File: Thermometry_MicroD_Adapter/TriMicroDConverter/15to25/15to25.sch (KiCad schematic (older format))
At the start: 3 parts, among them J1 Conn_02x05_Odd_Even, J2 DB15_Male, J4 DB25_Male

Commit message: update
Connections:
- net at J2.3: no longer J4.3
- net at J2.4: now also J4.3; no longer J4.4
- net at J2.5: now also J4.4; no longer J4.5
- net at J2.6: now also J4.5; no longer J4.6
- net at J2.7: now also J4.6
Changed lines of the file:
@@
 $EndComp
 Wire Wire Line
-	6500 2000 5950 2000
-Wire Wire Line
-	6500 2100 5950 2100
-Wire Wire Line
-	5950 2200 6500 2200
-Wire Wire Line
-	6500 2300 5950 2300
-Wire Wire Line
-	5950 2400 6500 2400
-Wire Wire Line
-	6500 2500 5950 2500
-Wire Wire Line
-	5950 2600 6500 2600
-Wire Wire Line
-	6500 2700 5950 2700
-Wire Wire Line
-	5950 2800 6500 2800
-Wire Wire Line
-	6500 2900 5950 2900
-Wire Wire Line
-	5950 3000 6500 3000
-Wire Wire Line
-	6500 3100 5950 3100
-Wire Wire Line
-	6500 3300 6700 3300
-Wire Wire Line
-	6700 3300 6700 3150
-Wire Wire Line
-	6700 3150 6100 3150
-Wire Wire Line
-	6100 3150 6100 3300
-Wire Wire Line
-	6100 3300 5950 3300
-NoConn ~ 5950 3200
-Wire Wire Line
-	6150 3200 6150 3350
-Wire Wire Line
-	6150 3350 5950 3350
-Wire Wire Line
 	5950 3350 5950 3400
-Wire Wire Line
-	6150 3200 6500 3200
 NoConn ~ 6500 4400
 $Comp
@@
 Wire Wire Line
 	5300 3800 5300 3750
+NoConn ~ 5950 2400
+Wire Wire Line
+	5950 2000 6500 2000
+Wire Wire Line
+	5950 2100 6500 2100
+Wire Wire Line
+	5950 2200 6500 2200
+Wire Wire Line
+	5950 2300 6500 2300
+Wire Wire Line
+	6500 2400 6150 2400
+Wire Wire Line
+	6150 2400 6150 2600
+Wire Wire Line
+	6150 2600 5950 2600
+Wire Wire Line
+	5950 2500 6500 2500
+Wire Wire Line
+	6500 2600 6200 2600
+Wire Wire Line
+	6200 2600 6200 2800
+Wire Wire Line
+	6200 2800 5950 2800
+Wire Wire Line
+	5950 2700 6500 2700
+Wire Wire Line
+	6500 2800 6250 2800
+Wire Wire Line
+	6250 2800 6250 3000
+Wire Wire Line
+	6250 3000 5950 3000
+Wire Wire Line
+	5950 2900 6500 2900
+Wire Wire Line
+	6500 3000 6300 3000
+Wire Wire Line
+	6300 3000 6300 3200
+Wire Wire Line
+	6300 3200 5950 3200
+Wire Wire Line
+	5950 3100 6500 3100
+Wire Wire Line
+	6500 3200 6350 3200
+Wire Wire Line
+	6350 3200 6350 3350
+Wire Wire Line
+	6350 3350 5950 3350
+Wire Wire Line
+	5950 3300 6500 3300
 $EndSCHEMATC

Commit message: update
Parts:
- removed J1: Conn_02x05_Odd_Even, Connector_PinHeader_1.00mm:PinHeader_2x05_P1.00mm_Vertical, symbol Connector_Generic:Conn_02x05_Odd_Even
- added J1, J3: Conn_01x04, Connector_JST:JST_PH_B4B-PH-K_1x04_P2.00mm_Vertical, symbol Connector_Generic:Conn_01x04
- added J5: Conn_01x02, Connector_PinHeader_1.00mm:PinHeader_1x02_P1.00mm_Vertical, symbol Connector_Generic:Conn_01x02
- J2: symbol Connector:DB15_Male -> Connector:DB15_Male_MountingHoles
- J4: symbol Connector:DB25_Male -> Connector:DB25_Male_MountingHoles
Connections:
- net at J4.10: now also J3.1 (Pin_1)
- net at J4.11: now also J3.3 (Pin_3)
- net at J4.12: now also J5.1 (Pin_1)
- net at J4.21 (P21): now also J1.2 (Pin_2)
- net at J4.22 (P22): now also J1.4 (Pin_4)
- net at J4.23 (P23): now also J3.2 (Pin_2)
- net at J4.24 (P24): now also J3.4 (Pin_4)
- net at J4.25 (P25): now also J5.2 (Pin_2)
- net at J4.8: now also J1.1 (Pin_1)
- net at J4.9: now also J1.3 (Pin_3)
- new net GND: J2.0 (PAD), J4.0 (PAD)
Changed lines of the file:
@@
 $EndDescr
 $Comp
-L Connector:DB25_Male J4
+L Connector:DB25_Male_MountingHoles J4
 U 1 1 610858EB
 P 6800 3200
@@
 $EndComp
 Wire Wire Line
+	6500 2000 5950 2000
+Wire Wire Line
+	6500 2100 5950 2100
+Wire Wire Line
+	5950 2200 6500 2200
+Wire Wire Line
+	6500 2300 5950 2300
+Wire Wire Line
+	6500 2500 5950 2500
+Wire Wire Line
+	6500 2700 5950 2700
+Wire Wire Line
+	6500 2900 5950 2900
+Wire Wire Line
+	6500 3100 5950 3100
+Wire Wire Line
 	5950 3350 5950 3400
 NoConn ~ 6500 4400
 $Comp
-L Connector_Generic:Conn_02x05_Odd_Even J1
-U 1 1 610B8918
-P 5600 3950
-F 0 "J1" H 5650 4367 50  0000 C CNN
-F 1 "Conn_02x05_Odd_Even" H 5650 4276 50  0000 C CNN
-F 2 "Connector_PinHeader_1.00mm:PinHeader_2x05_P1.00mm_Vertical" H 5600 3950 50  0001 C CNN
-F 3 "~" H 5600 3950 50  0001 C CNN
-	1    5600 3950
-	-1   0    0    -1
-$EndComp
-$Comp
-L Connector:DB15_Male J2
+L Connector:DB15_Male_MountingHoles J2
 U 1 1 61081BFB
 P 5650 2700
@@
 	6000 3400 6000 3750
 Wire Wire Line
-	6000 3750 5800 3750
-Wire Wire Line
 	6500 3600 6100 3600
-Wire Wire Line
-	6100 3600 6100 3850
-Wire Wire Line
-	6100 3850 5800 3850
 Wire Wire Line
 	6500 3800 6200 3800
 Wire Wire Line
-	6200 3800 6200 3950
-Wire Wire Line
-	6200 3950 5800 3950
-Wire Wire Line
 	6500 4000 6300 4000
-Wire Wire Line
-	6300 4000 6300 4050
-Wire Wire Line
-	6300 4050 5800 4050
-Wire Wire Line
-	6500 4200 5800 4200
-Wire Wire Line
-	5800 4200 5800 4150
-Wire Wire Line
-	5300 4150 5300 4300
-Wire Wire Line
-	5300 4300 6500 4300
-Wire Wire Line
-	6500 4100 5300 4100
-Wire Wire Line
-	5300 4100 5300 4050
 Wire Wire Line
 	6500 3900 6250 3900
 Wire Wire Line
-	6250 3900 6250 4000
-Wire Wire Line
-	6250 4000 5300 4000
-Wire Wire Line
-	5300 4000 5300 3950
-Wire Wire Line
 	6500 3700 6150 3700
-Wire Wire Line
-	6150 3700 6150 3900
-Wire Wire Line
-	6150 3900 5300 3900
-Wire Wire Line
-	5300 3900 5300 3850
 Wire Wire Line
 	6500 3500 6050 3500
 Wire Wire Line
-	6050 3500 6050 3800
+	5950 2600 6000 2600
 Wire Wire Line
-	6050 3800 5300 3800
+	6000 2600 6000 2400
 Wire Wire Line
-	5300 3800 5300 3750
+	6000 2400 6500 2400
+Wire Wire Line
+	5950 2800 6050 2800
+Wire Wire Line
+	6050 2800 6050 2600
+Wire Wire Line
+	6050 2600 6500 2600
+Wire Wire Line
+	5950 3000 6100 3000
+Wire Wire Line
+	6100 3000 6100 2800
+Wire Wire Line
+	6100 2800 6500 2800
+Wire Wire Line
+	5950 3300 6500 3300
+Wire Wire Line
+	5950 3200 6150 3200
+Wire Wire Line
+	6150 3200 6150 3000
+Wire Wire Line
+	6150 3000 6500 3000
+Wire Wire Line
+	5950 3350 6200 3350
+Wire Wire Line
+	6200 3350 6200 3200
+Wire Wire Line
+	6200 3200 6500 3200
 NoConn ~ 5950 2400
 Wire Wire Line
-	5950 2000 6500 2000
+	5650 1800 5650 1500
 Wire Wire Line
-	5950 2100 6500 2100
+	5650 1500 6800 1500
 Wire Wire Line
-	5950 2200 6500 2200
+	6800 1500 6800 1800
+$Comp
+L power:GND #PWR0101
+U 1 1 62D0C880
+P 7050 1500
+F 0 "#PWR0101" H 7050 1250 50  0001 C CNN
+F 1 "GND" H 7055 1327 50  0000 C CNN
+F 2 "" H 7050 1500 50  0001 C CNN
+F 3 "" H 7050 1500 50  0001 C CNN
+	1    7050 1500
+	1    0    0    -1
+$EndComp
 Wire Wire Line
-	5950 2300 6500 2300
+	6800 1500 7050 1500
+Connection ~ 6800 1500
+$Comp
+L Connector_Generic:Conn_01x02 J5
+U 1 1 62CF5D5C
+P 5850 4700
+F 0 "J5" H 6150 4750 50  0000 C CNN
+F 1 "Conn_01x02" H 6150 4650 50  0000 C CNN
+F 2 "Connector_PinHeader_1.00mm:PinHeader_1x02_P1.00mm_Vertical" H 5850 4700 50  0001 C CNN
+F 3 "~" H 5850 4700 50  0001 C CNN
+	1    5850 4700
+	-1   0    0    -1
+$EndComp
 Wire Wire Line
-	6500 2400 6150 2400
+	6000 3750 5700 3750
 Wire Wire Line
-	6150 2400 6150 2600
+	6050 3850 5700 3850
 Wire Wire Line
-	6150 2600 5950 2600
+	6050 3500 6050 3850
 Wire Wire Line
-	5950 2500 6500 2500
+	5700 3950 6100 3950
 Wire Wire Line
-	6500 2600 6200 2600
+	6100 3600 6100 3950
 Wire Wire Line
-	6200 2600 6200 2800
+	5700 4050 6150 4050
 Wire Wire Line
-	6200 2800 5950 2800
+	6150 3700 6150 4050
 Wire Wire Line
-	5950 2700 6500 2700
+	5700 4150 6200 4150
 Wire Wire Line
-	6500 2800 6250 2800
+	6200 3800 6200 4150
 Wire Wire Line
-	6250 2800 6250 3000
+	5700 4250 6250 4250
 Wire Wire Line
-	6250 3000 5950 3000
+	6250 3900 6250 4250
 Wire Wire Line
-	5950 2900 6500 2900
+	5700 4350 6300 4350
 Wire Wire Line
-	6500 3000 6300 3000
+	6300 4000 6300 4350
 Wire Wire Line
-	6300 3000 6300 3200
+	6350 4450 6350 4100
 Wire Wire Line
-	6300 3200 5950 3200
+	6350 4100 6500 4100
 Wire Wire Line
-	5950 3100 6500 3100
+	5700 4450 6350 4450
 Wire Wire Line
-	6500 3200 6350 3200
+	6050 4700 6400 4700
 Wire Wire Line
-	6350 3200 6350 3350
+	6400 4700 6400 4200
 Wire Wire Line
-	6350 3350 5950 3350
+	6400 4200 6500 4200
 Wire Wire Line
-	5950 3300 6500 3300
+	6500 4300 6450 4300
+Wire Wire Line
+	6450 4300 6450 4800
+Wire Wire Line
+	6450 4800 6050 4800
+$Comp
+L Connector_Generic:Conn_01x04 J1
+U 1 1 62D54AD7
+P 5500 3850
+F 0 "J1" H 5418 4167 50  0000 C CNN
+F 1 "Conn_01x04" H 5418 4076 50  0000 C CNN
+F 2 "Connector_JST:JST_PH_B4B-PH-K_1x04_P2.00mm_Vertical" H 5500 3850 50  0001 C CNN
+F 3 "~" H 5500 3850 50  0001 C CNN
+F 4 "C566009" H 5500 3850 50  0001 C CNN "LCSC"
+	1    5500 3850
+	-1   0    0    -1
+$EndComp
+$Comp
+L Connector_Generic:Conn_01x04 J3
+U 1 1 62D59C75
+P 5500 4250
+F 0 "J3" H 5850 4250 50  0000 C CNN
+F 1 "Conn_01x04" H 5900 4100 50  0000 C CNN
+F 2 "Connector_JST:JST_PH_B4B-PH-K_1x04_P2.00mm_Vertical" H 5500 4250 50  0001 C CNN
+F 3 "~" H 5500 4250 50  0001 C CNN
+F 4 "C566009" H 5500 4250 50  0001 C CNN "LCSC"
+	1    5500 4250
+	-1   0    0    -1
+$EndComp
 $EndSCHEMATC

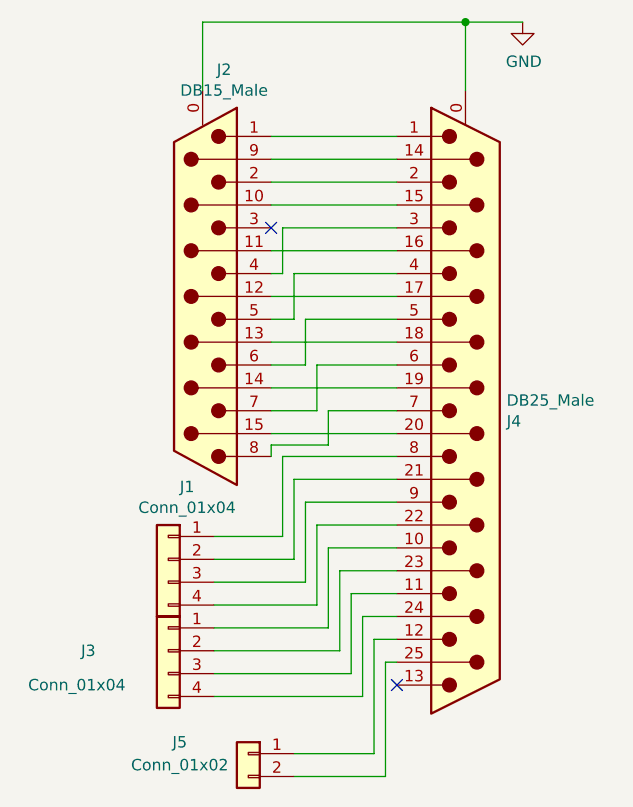
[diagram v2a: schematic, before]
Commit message: Fixed Error in board. Added diagrams
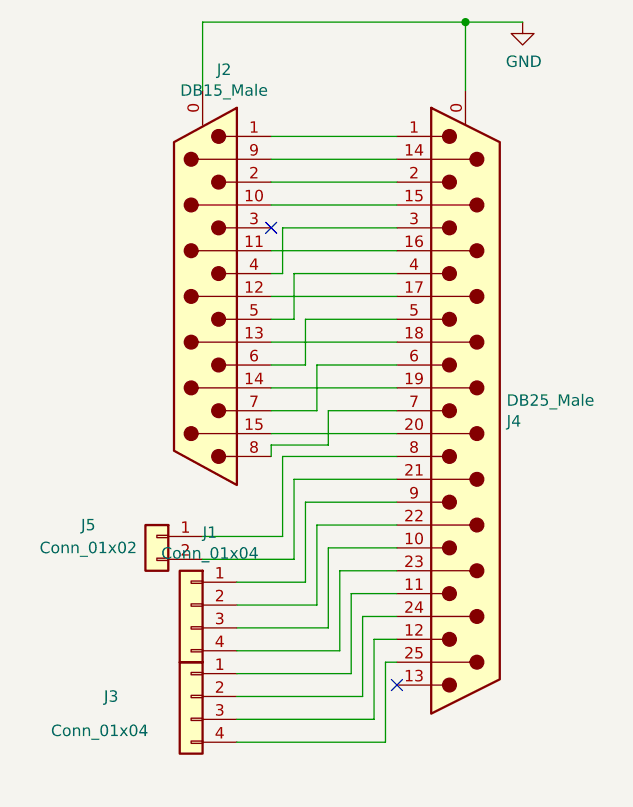
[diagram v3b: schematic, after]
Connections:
- net at J4.10: now also J1.3 (Pin_3); no longer J3.1 (Pin_1)
- net at J4.11: now also J3.1 (Pin_1); no longer J3.3 (Pin_3)
- net at J4.12: now also J3.3 (Pin_3); no longer J5.1 (Pin_1)
- net at J4.21 (P21): now also J5.2 (Pin_2); no longer J1.2 (Pin_2)
- net at J4.22 (P22): now also J1.2 (Pin_2); no longer J1.4 (Pin_4)
- net at J4.23 (P23): now also J1.4 (Pin_4); no longer J3.2 (Pin_2)
- net at J4.24 (P24): now also J3.2 (Pin_2); no longer J3.4 (Pin_4)
- net at J4.25 (P25): now also J3.4 (Pin_4); no longer J5.2 (Pin_2)
- net at J4.8: now also J5.1 (Pin_1); no longer J1.1 (Pin_1)
- net at J4.9: now also J1.1 (Pin_1); no longer J1.3 (Pin_3)
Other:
- moved on the sheet: J1, J3, J5
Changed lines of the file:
@@
 	6800 1500 7050 1500
 Connection ~ 6800 1500
-$Comp
-L Connector_Generic:Conn_01x02 J5
-U 1 1 62CF5D5C
-P 5850 4700
-F 0 "J5" H 6150 4750 50  0000 C CNN
-F 1 "Conn_01x02" H 6150 4650 50  0000 C CNN
-F 2 "Connector_PinHeader_1.00mm:PinHeader_1x02_P1.00mm_Vertical" H 5850 4700 50  0001 C CNN
-F 3 "~" H 5850 4700 50  0001 C CNN
-	1    5850 4700
-	-1   0    0    -1
-$EndComp
-Wire Wire Line
-	6000 3750 5700 3750
-Wire Wire Line
-	6050 3850 5700 3850
 Wire Wire Line
 	6050 3500 6050 3850
 Wire Wire Line
-	5700 3950 6100 3950
-Wire Wire Line
 	6100 3600 6100 3950
-Wire Wire Line
-	5700 4050 6150 4050
 Wire Wire Line
 	6150 3700 6150 4050
 Wire Wire Line
-	5700 4150 6200 4150
-Wire Wire Line
 	6200 3800 6200 4150
 Wire Wire Line
-	5700 4250 6250 4250
-Wire Wire Line
 	6250 3900 6250 4250
-Wire Wire Line
-	5700 4350 6300 4350
 Wire Wire Line
 	6300 4000 6300 4350
@@
 	6350 4100 6500 4100
 Wire Wire Line
-	5700 4450 6350 4450
-Wire Wire Line
-	6050 4700 6400 4700
-Wire Wire Line
-	6400 4700 6400 4200
-Wire Wire Line
 	6400 4200 6500 4200
 Wire Wire Line
 	6500 4300 6450 4300
+$Comp
+L Connector_Generic:Conn_01x02 J5
+U 1 1 62CF5D5C
+P 5450 3750
+F 0 "J5" H 5750 3800 50  0000 C CNN
+F 1 "Conn_01x02" H 5750 3700 50  0000 C CNN
+F 2 "Connector_PinHeader_1.00mm:PinHeader_1x02_P1.00mm_Vertical" H 5450 3750 50  0001 C CNN
+F 3 "~" H 5450 3750 50  0001 C CNN
+	1    5450 3750
+	-1   0    0    -1
+$EndComp
 Wire Wire Line
-	6450 4300 6450 4800
+	5650 3750 6000 3750
 Wire Wire Line
-	6450 4800 6050 4800
+	6050 3850 5650 3850
+Wire Wire Line
+	6100 3950 5800 3950
+Wire Wire Line
+	6150 4050 5800 4050
+Wire Wire Line
+	5800 4150 6200 4150
+Wire Wire Line
+	5800 4250 6250 4250
+Wire Wire Line
+	5800 4350 6300 4350
+Wire Wire Line
+	5800 4450 6350 4450
+Wire Wire Line
+	5800 4550 6400 4550
+Wire Wire Line
+	5800 4650 6450 4650
 $Comp
 L Connector_Generic:Conn_01x04 J1
 U 1 1 62D54AD7
-P 5500 3850
-F 0 "J1" H 5418 4167 50  0000 C CNN
-F 1 "Conn_01x04" H 5418 4076 50  0000 C CNN
-F 2 "Connector_JST:JST_PH_B4B-PH-K_1x04_P2.00mm_Vertical" H 5500 3850 50  0001 C CNN
-F 3 "~" H 5500 3850 50  0001 C CNN
-F 4 "C566009" H 5500 3850 50  0001 C CNN "LCSC"
-	1    5500 3850
+P 5600 4050
+F 0 "J1" H 5518 4367 50  0000 C CNN
+F 1 "Conn_01x04" H 5518 4276 50  0000 C CNN
+F 2 "Connector_JST:JST_PH_B4B-PH-K_1x04_P2.00mm_Vertical" H 5600 4050 50  0001 C CNN
+F 3 "~" H 5600 4050 50  0001 C CNN
+F 4 "C566009" H 5600 4050 50  0001 C CNN "LCSC"
+	1    5600 4050
 	-1   0    0    -1
 $EndComp
@@
 L Connector_Generic:Conn_01x04 J3
 U 1 1 62D59C75
-P 5500 4250
-F 0 "J3" H 5850 4250 50  0000 C CNN
-F 1 "Conn_01x04" H 5900 4100 50  0000 C CNN
-F 2 "Connector_JST:JST_PH_B4B-PH-K_1x04_P2.00mm_Vertical" H 5500 4250 50  0001 C CNN
-F 3 "~" H 5500 4250 50  0001 C CNN
-F 4 "C566009" H 5500 4250 50  0001 C CNN "LCSC"
-	1    5500 4250
+P 5600 4450
+F 0 "J3" H 5950 4450 50  0000 C CNN
+F 1 "Conn_01x04" H 6000 4300 50  0000 C CNN
+F 2 "Connector_JST:JST_PH_B4B-PH-K_1x04_P2.00mm_Vertical" H 5600 4450 50  0001 C CNN
+F 3 "~" H 5600 4450 50  0001 C CNN
+F 4 "C566009" H 5600 4450 50  0001 C CNN "LCSC"
+	1    5600 4450
 	-1   0    0    -1
 $EndComp
+Wire Wire Line
+	6400 4550 6400 4200
+Wire Wire Line
+	6450 4300 6450 4650
 $EndSCHEMATC
